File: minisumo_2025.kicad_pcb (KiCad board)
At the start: 2 copper layers, 40.2 x 90 mm, 65 parts, among them J1 USB_C Connector, J10 DISTANCE_R90, J11 DISTANCE_R, J12 DISTANCE_RF, J13 DISTANCE_L90, J14 DISTANCE_L, J15 LINE_LEFT, J16 DISTANCE_LF, J2 SERVO, J3 START_MODULE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

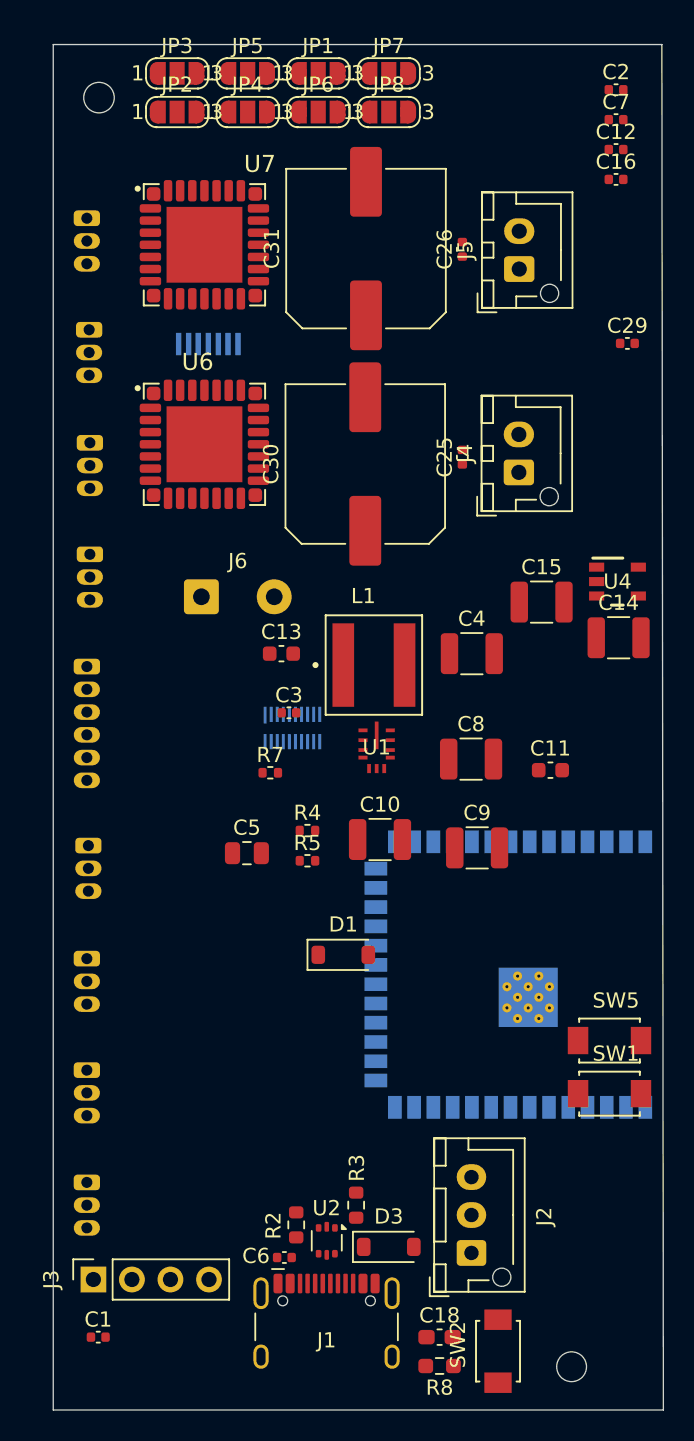
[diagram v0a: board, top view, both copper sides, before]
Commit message: added connectors and 3D models
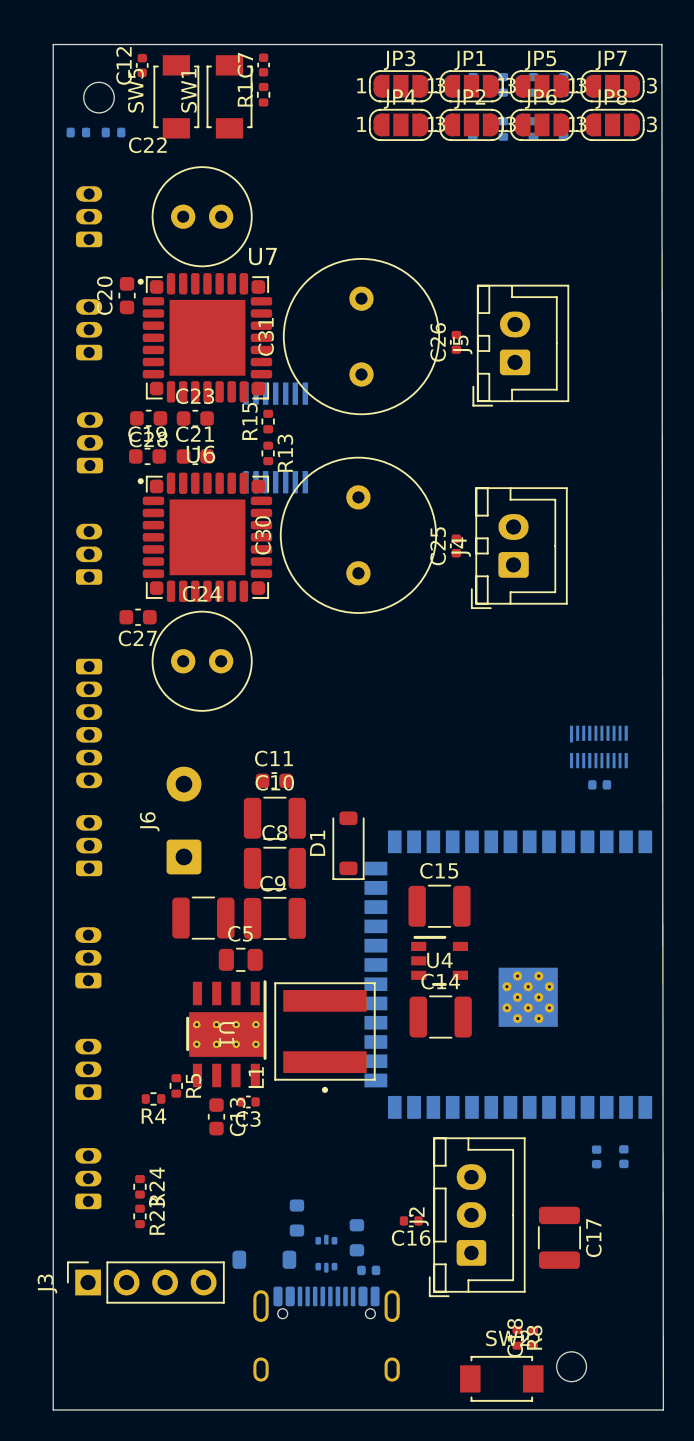
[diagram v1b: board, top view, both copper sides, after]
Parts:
- removed R7: 100k, Resistor_SMD:R_0402_1005Metric
- added C17: 10uF, Capacitor_SMD:C_1210_3225Metric, F.Cu at (143.8, 127.1)
- added C19: 33nF, Capacitor_SMD:C_0603_1608Metric, F.Cu at (116.6, 75.6)
- added C20: 33nF, Capacitor_SMD:C_0603_1608Metric, F.Cu at (115.2, 65.0)
- added C21: 100nF, Capacitor_SMD:C_0603_1608Metric, F.Cu at (119.8, 75.6)
- added C22: 100uF, Capacitor_THT:C_Radial_D6.3mm_H11.0mm_P2.50mm, F.Cu at (119.0, 59.8)
- added C23: 100nF, Capacitor_SMD:C_0603_1608Metric, F.Cu at (119.8, 73.1)
- added C24: 100uF, Capacitor_THT:C_Radial_D6.3mm_H11.0mm_P2.50mm, F.Cu at (119.0, 89.1)
- added C27: 100nF, Capacitor_SMD:C_0603_1608Metric, F.Cu at (116.0, 86.2)
- added C28: 100nF, Capacitor_SMD:C_0603_1608Metric, F.Cu at (116.7, 73.1)
- added R1: 10k, Resistor_SMD:R_0402_1005Metric, F.Cu at (124.2, 51.8)
- added R10: 1k, Resistor_SMD:R_0402_1005Metric, B.Cu at (140.1, 51.1)
- added R11: 1k, Resistor_SMD:R_0402_1005Metric, B.Cu at (142.0, 51.1)
- added R12: 1k, Resistor_SMD:R_0402_1005Metric, B.Cu at (144.0, 51.1)
- added R13: 10k, Resistor_SMD:R_0402_1005Metric, F.Cu at (124.5, 75.4)
- added R14: 1k, Resistor_SMD:R_0402_1005Metric, B.Cu at (138.0, 54.0)
- added R15: 10k, Resistor_SMD:R_0402_1005Metric, F.Cu at (124.5, 73.3)
- added R16: 1k, Resistor_SMD:R_0402_1005Metric, B.Cu at (140.1, 54.0)
- added R19: 1k, Resistor_SMD:R_0402_1005Metric, B.Cu at (142.0, 54.0)
- added R20: 1k, Resistor_SMD:R_0402_1005Metric, B.Cu at (144.0, 54.0)
- added R21: 2k, Resistor_SMD:R_0402_1005Metric, B.Cu at (112.0, 54.2)
- added R22: 3.3k, Resistor_SMD:R_0402_1005Metric, B.Cu at (114.4, 54.2)
- added R23: 2k, Resistor_SMD:R_0402_1005Metric, F.Cu at (116.1, 125.7)
- added R24: 3.3k, Resistor_SMD:R_0402_1005Metric, F.Cu at (116.1, 123.7)
- added R9: 1k, Resistor_SMD:R_0402_1005Metric, B.Cu at (138.1, 51.1)
- C1, C2, C29, C6, D3, J1, R2, R3, U2: moved to B.Cu
- C18: footprint Capacitor_SMD:C_0603_1608Metric_Pad1.08x0.95mm_HandSolder -> Capacitor_SMD:C_0402_1005Metric
- C30, C31: footprint Capacitor_SMD:C_Elec_10x10.2 -> Capacitor_THT:C_Radial_D10.0mm_H16.0mm_P5.00mm
- J10, J11, J12, J13, J14, J15, J16, J9: footprint Connector_JST:JST_ZH_B3B-ZR_1x03_P1.50mm_Vertical -> Connector_JST:CONN-TH_S3B-ZR-3.4-LF-SN
- J2: footprint Connector_JST:JST_XH_B3B-XH-AM_1x03_P2.50mm_Vertical -> Connector_JST:JST_XH_B3B-XH-A_1x03_P2.50mm_Vertical
- J4, J5: footprint Connector_JST:JST_XH_B2B-XH-AM_1x02_P2.50mm_Vertical -> Connector_JST:JST_XH_B2B-XH-A_1x02_P2.50mm_Vertical
- R8: value 5K -> 5k; footprint Resistor_SMD:R_0603_1608Metric_Pad0.98x0.95mm_HandSolder -> Resistor_SMD:R_0402_1005Metric
- U1: value LMR33630ARNXR -> LMR33630ADDAR; footprint footprints:RNX0012B -> footprints:DDA0008J
- moved C2 70.4 mm to (146.2, 121.8), turned to 90 degrees
- moved SW1 70.3 mm to (122.0, 51.9), turned to 90 degrees
- moved C16 70.0 mm to (134.0, 126.0), turned to 180 degrees
- moved SW5 68.4 mm to (118.5, 51.9), turned to 90 degrees
- moved C1 36.6 mm to (148.0, 121.8), turned to 90 degrees
- moved C12 31.7 mm to (116.2, 49.8), turned to 90 degrees
- moved C13 30.8 mm to (121.1, 119.1), turned to -90 degrees
- moved C29 29.2 mm to (146.4, 97.2)
- moved C14 27.6 mm to (135.9, 112.5)
- moved U4 27.6 mm to (135.8, 108.8)
- moved J12 26.7 mm to (112.8, 82.0), turned to 90 degrees
- moved C3 25.8 mm to (123.2, 118.2), turned to 180 degrees
- moved C4 24.8 mm to (120.3, 106.0)
- moved L1 24.4 mm to (128.3, 113.5), turned to 90 degrees
- moved C7 23.5 mm to (124.2, 49.8), turned to 90 degrees
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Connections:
- C3 pad 2: Net-(U1-BST) -> Net-(U1-BOOT)
- U1 pad 3: unconnected-(U1-NC-Pad3) -> +BATT
- U1 pad 4: Net-(U1-BST) -> unconnected-(U1-PG-Pad4)
- U1 pad 5: Net-(U1-VCC) -> Net-(U1-FB)
- U1 pad 6: GND -> Net-(U1-VCC)
- U1 pad 7: Net-(U1-FB) -> Net-(U1-BOOT)
- U1 pad 8: Net-(U1-PG) -> Net-(U1-SW)
- U1 pad 9: +BATT -> GND
- U6 pad 8: Net-(U6-FB) -> unconnected-(U6-FB-Pad8)
- U7 pad 8: Net-(U7-FB) -> unconnected-(U7-FB-Pad8)

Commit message: base layout
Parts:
- removed U8: TXS0108ERGYR, footprints:DQS20_TEX
- added C32: 1uF, Capacitor_SMD:C_0402_1005Metric, B.Cu at (146.4, 120.0)
- added C33: 0.1uF, Capacitor_SMD:C_0402_1005Metric, B.Cu at (131.7, 92.0)
- added R7: 10k, Resistor_SMD:R_0402_1005Metric, F.Cu at (122.1, 131.8)
- C2: value 0.1uF -> 10uF
- J10, J11, J12, J13, J14, J15, J16, J9: footprint Connector_JST:CONN-TH_S3B-ZR-3.4-LF-SN -> footprints:CONN-TH_S3B-ZR-3.4-LF-SN
- J8: footprint Connector_JST:JST_ZH_B6B-ZR_1x06_P1.50mm_Vertical -> footprints:CONN-TH_S6B-ZR-3.4-LF-SN
- R10, R11, R12, R14, R16, R19, R20, R9: moved to F.Cu
- U5: value ~ -> TXS0108ERGYR; footprint footprints:SOP65P640X120-14N -> footprints:DQS20_TEX
- moved SW1 83.5 mm to (126.0, 135.3)
- moved SW5 83.5 mm to (121.2, 135.3)
- moved C12 82.1 mm to (120.2, 131.8), turned to 0 degrees
- moved C7 82.1 mm to (125.1, 131.8), turned to 0 degrees
- moved R1 80.1 mm to (127.0, 131.8), turned to 180 degrees
- moved C18 27.0 mm to (115.1, 131.8), turned to 180 degrees
- moved R8 24.0 mm to (117.0, 131.8), turned to 180 degrees
- moved SW2 23.8 mm to (116.2, 135.3), turned to 90 degrees
- moved U5 20.1 mm to (133.9, 92.5), turned to 180 degrees
- moved R12 16.2 mm to (128.3, 55.1), turned to 0 degrees
- moved C15 14.6 mm to (130.5, 118.8), turned to -90 degrees
- moved C14 14.2 mm to (123.2, 118.9), turned to -90 degrees
- moved U4 13.4 mm to (126.9, 118.8), turned to -90 degrees
- moved R11 12.4 mm to (130.2, 55.1), turned to 180 degrees
- moved C29 11.6 mm to (136.1, 92.0), turned to 90 degrees
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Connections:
- C19 pad 1: +BATT -> +3V3
- C27 pad 1: +5V -> +3V3
- C28 pad 1: +5V -> +3V3
- J6 pad 1: +BATT -> GND
- J6 pad 2: GND -> +BATT
- R13 pad 1: +5V -> +3V3
- R15 pad 1: +5V -> +3V3
- U2 pad 1: /D- -> /D+
- U2 pad 3: /D+ -> /D-
- U2 pad 4: /D_P -> /D_N
- U2 pad 6: /D_N -> /D_P
- U3 pad 10: unconnected-(U3-IO17-Pad10) -> /GPIO17
- U3 pad 11: unconnected-(U3-IO18-Pad11) -> /GPIO18
- U3 pad 12: unconnected-(U3-IO8-Pad12) -> /GPIO8
- U3 pad 17: unconnected-(U3-IO9-Pad17) -> /GPIO9
- U3 pad 18: unconnected-(U3-IO10-Pad18) -> /GPIO10
- U3 pad 19: unconnected-(U3-IO11-Pad19) -> /GPIO11
- U3 pad 20: unconnected-(U3-IO12-Pad20) -> /GPIO12
- U3 pad 21: unconnected-(U3-IO13-Pad21) -> /GPIO13
- U3 pad 22: unconnected-(U3-IO14-Pad22) -> /GPIO14
- U3 pad 23: unconnected-(U3-IO21-Pad23) -> /GPIO21
- U3 pad 24: unconnected-(U3-IO47-Pad24) -> /GPIO47
- U3 pad 25: unconnected-(U3-IO48-Pad25) -> /GPIO48
- U3 pad 28: unconnected-(U3-IO35-Pad28) -> /GPIO35
- U3 pad 29: unconnected-(U3-IO36-Pad29) -> /GPIO36
- U3 pad 30: unconnected-(U3-IO37-Pad30) -> /GPIO37
- U3 pad 31: unconnected-(U3-IO38-Pad31) -> /GPIO38
- U3 pad 38: unconnected-(U3-IO2-Pad38) -> /GPIO2
- U3 pad 39: unconnected-(U3-IO1-Pad39) -> /GPIO1
- U3 pad 4: unconnected-(U3-IO4-Pad4) -> /GPIO4
- U3 pad 5: unconnected-(U3-IO5-Pad5) -> /GPIO5
- U3 pad 6: unconnected-(U3-IO6-Pad6) -> /GPIO6
- U3 pad 7: unconnected-(U3-IO7-Pad7) -> /GPIO7
- U3 pad 8: unconnected-(U3-IO15-Pad8) -> /GPIO15
- U3 pad 9: unconnected-(U3-IO16-Pad9) -> /GPIO16
- U5 pad 1: GND -> /DISTANCE_R90
- U5 pad 10: GND -> unconnected-(U5-A8-Pad10)
- U5 pad 11: /IN1_2 -> unconnected-(U5-B8-Pad11)
- U5 pad 12: /IN1_2_ESP -> /DISTANCE_L90_OUT
- U5 pad 13: GND -> /DISTANCE_L_OUT
- U5 pad 14: +5V -> /DISTANCE_LF_OUT
- U5 pad 2: /IN1_1_ESP -> /DISTANCE_R
- U5 pad 3: /IN1_1 -> /DISTANCE_RF
- U5 pad 5: /IN2_1_ESP -> +3V3
- U5 pad 6: /IN2_1 -> unconnected-(U5-OE-Pad6)
- U5 pad 7: GND -> /DISTANCE_LF
- U5 pad 8: /IN2_2 -> /DISTANCE_L
- U5 pad 9: /IN2_2_ESP -> /DISTANCE_L90
- U6 pad 10: +5V -> +3V3
- U7 pad 10: +5V -> +3V3
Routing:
- net /D-: track 0.00 -> 9.05 mm
- net /D+: track 0.00 -> 9.05 mm
- net +3V3: track 0.00 -> 2.53 mm
- net /ESP_EN: track 0.00 -> 1.54 mm
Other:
- board size 40.2 x 90 mm -> 40.1 x 90 mm
- copper layers 2 -> 4

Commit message: changes
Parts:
- moved R22 1.19 mm to (114.5, 55.9)
- moved R14 0.27 mm to (142.9, 55.2)
- moved R19 0.26 mm to (148.9, 55.2)
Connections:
- U1 pad V: (no net) -> GND
- U6 pad 1: /IN2_1 -> /GPIO37
- U6 pad 2: /IN1_1 -> /GPIO38
- U7 pad 1: /IN2_2 -> /GPIO1
- U7 pad 2: /IN1_2 -> /GPIO2
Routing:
- net /INV_1: track 0.00 -> 6.38 mm
- net /ND2_1: track 0.00 -> 6.23 mm
- net /SLEW_1: track 0.00 -> 6.23 mm
- net /LINE_RIGHT_OUT: track 0.00 -> 6.17 mm
- net /D1_1: track 0.00 -> 6.00 mm
- net /LINE_RIGHT: track 0.00 -> 1.96 mm
- net /INV_2: track 0.00 -> 1.77 mm
- net /SLEW_2: track 0.00 -> 1.77 mm
- net /ND2_2: track 0.00 -> 1.76 mm
- net /D1_2: track 0.00 -> 1.76 mm
- added copper zone on In1.Cu, net GND

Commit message: regulator routing
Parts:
- moved C11 11.9 mm to (126.0, 103.8)
- moved D1 4.10 mm to (133.0, 94.4), turned to 180 degrees
- moved C29 4.09 mm to (139.4, 89.6)
- moved C33 4.09 mm to (135.0, 89.7)
- moved U5 4.09 mm to (137.2, 90.1)
- moved J6 4.01 mm to (119.0, 93.5), turned to -90 degrees
- moved R4 2.04 mm to (117.7, 110.8), turned to 90 degrees
- moved R1 1.76 mm to (126.9, 133.6), turned to 90 degrees
- moved C1 1.50 mm to (147.1, 120.0)
- moved C2 1.50 mm to (147.1, 121.0)
- moved C32 1.50 mm to (144.9, 120.0)
- moved C6 1.50 mm to (134.8, 129.2)
- moved J1 1.50 mm to (132.1, 134.7)
- moved R2 1.50 mm to (134.1, 127.0)
- moved R3 1.50 mm to (130.1, 125.8)
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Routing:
- net Net-(D1-A): track 0.00 -> 21.3 mm, vias 0 -> 2
- net Net-(U1-FB): track 0.00 -> 2.47 mm
- net Net-(U1-VCC): track 0.00 -> 1.96 mm
- net Net-(U1-BOOT): track 0.00 -> 1.89 mm
- net GND: vias 0 -> 3
- added copper zone on F.Cu, net +BATT
- added copper zone on B.Cu, net GND
- added copper zone on F.Cu, net GND
- added copper zone on F.Cu, net Net-(D1-A)
- added copper zone on F.Cu, net Net-(U1-SW)
- removed copper zone on In1.Cu, net GND

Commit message: minor adjustment
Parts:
- moved R1 1.76 mm to (127.0, 131.8), turned to 180 degrees
- moved C1 1.50 mm to (148.6, 120.0)
- moved C2 1.50 mm to (148.6, 121.0)
- moved C32 1.50 mm to (146.4, 120.0)
- moved C6 1.50 mm to (136.3, 129.2)
- moved J1 1.50 mm to (133.6, 134.7)
- moved R2 1.50 mm to (135.6, 127.0)
- moved R3 1.50 mm to (131.6, 125.8)
- moved U2 1.50 mm to (133.5, 128.1)
- moved U3 1.50 mm to (144.2, 109.8)
- moved D3 1.50 mm to (129.4, 128.5)
- moved SW1 1.45 mm to (126.0, 135.3)
- moved C7 0.06 mm to (125.1, 131.8), turned to 0 degrees

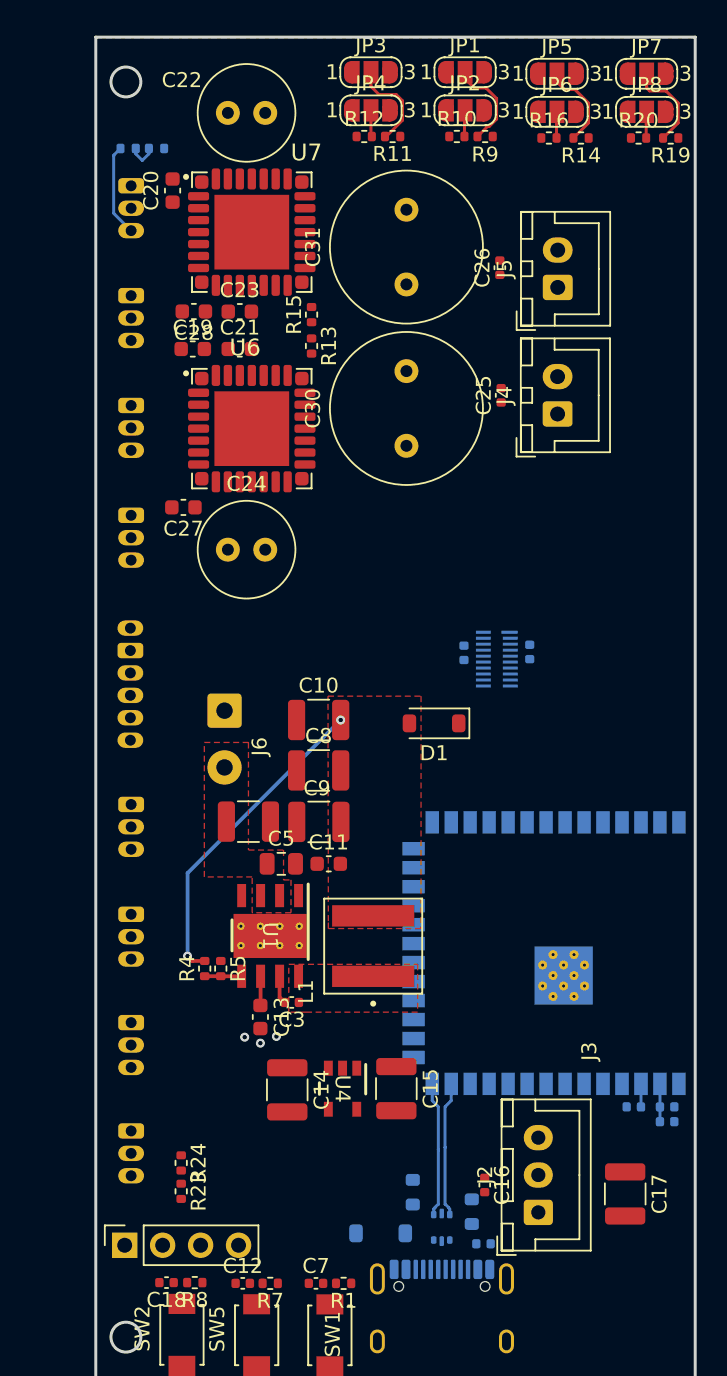
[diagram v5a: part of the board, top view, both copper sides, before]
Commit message: motor driver traces
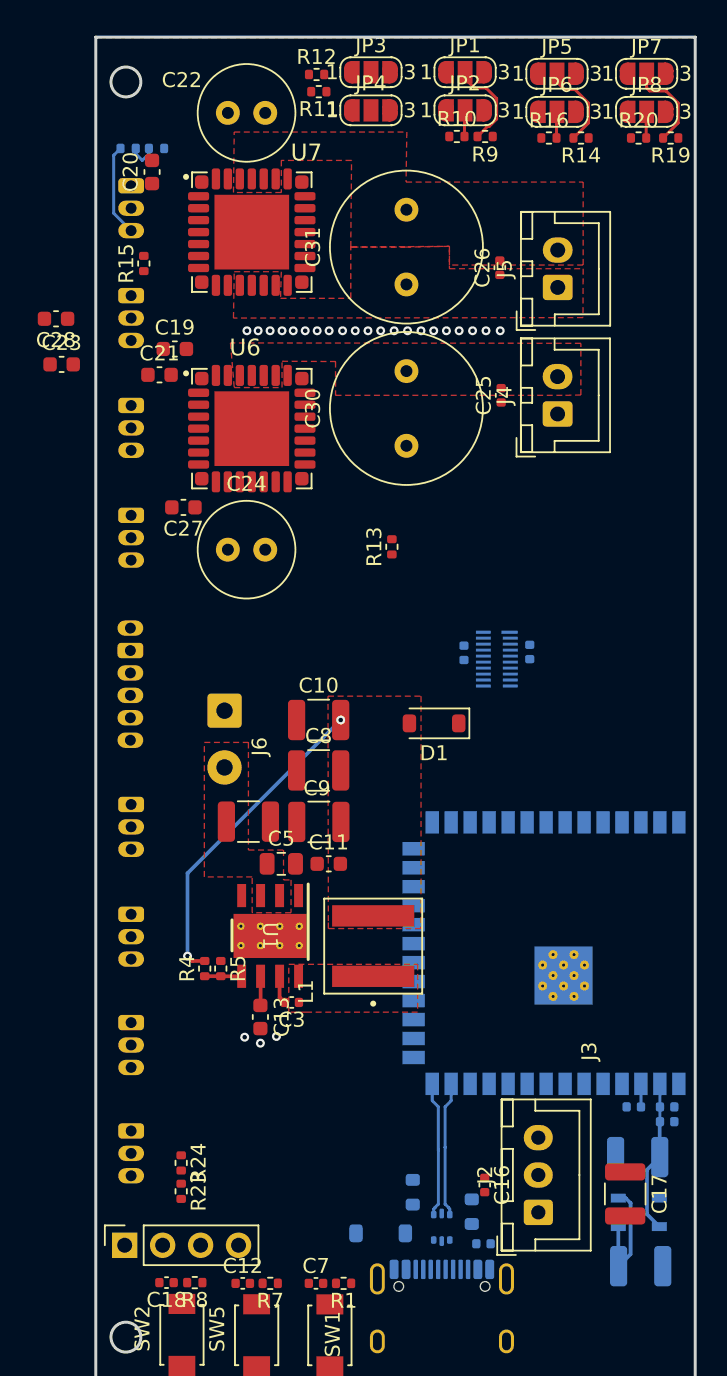
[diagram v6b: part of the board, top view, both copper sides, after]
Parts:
- C14, C15, U4: moved to B.Cu
- moved C14 23.9 mm to (146.7, 123.4), turned to 0 degrees
- moved U4 21.5 mm to (146.7, 127.1), turned to 0 degrees
- moved C15 20.2 mm to (146.8, 130.7), turned to 180 degrees
- moved R13 14.5 mm to (130.2, 82.6), turned to 90 degrees
- moved C23 12.4 mm to (108.1, 70.3)
- moved R15 11.7 mm to (113.6, 63.6)
- moved C28 9.24 mm to (107.7, 67.3)
- moved R11 5.78 mm to (125.3, 52.1)
- moved C21 5.65 mm to (114.7, 71.0)
- moved R12 5.23 mm to (125.2, 51.0)
- moved C20 1.85 mm to (114.2, 57.5)
- moved C19 1.20 mm to (115.7, 69.3)
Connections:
- U1 pad V: GND -> (no net)
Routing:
- net +5V: track 0.00 -> 8.18 mm
- net +3V3: track 2.53 -> 10.3 mm
- net /INV_1: track 6.38 -> 0.00 mm
- net /INV_2: track 1.77 -> 0.00 mm
- net GND: vias 3 -> 24
- added copper zone on F.Cu, net /MOTOR1_B
- added copper zone on F.Cu, net /MOTOR2_A
- added copper zone on F.Cu, net /MOTOR2_B
